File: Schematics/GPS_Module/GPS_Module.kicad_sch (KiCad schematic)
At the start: 21 parts, among them U1 STM32F103CBTx, U2 ISO1042BQDWVQ1, U3 SAM-M10Q, Y1 16MHz

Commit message: added notes
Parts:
- removed D3: STATUS_LED, LED_SMD:LED_0805_2012Metric, symbol Device:LED
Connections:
- net +3.3V: now also C1.2, C2.2, U2.1 (VCC1), U2.4 (GND1), U2.8 (VCC2); no longer U2.5 (GND2)
- net GND1: now also U2.5 (GND2); no longer U2.4 (GND1)
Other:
- note added: "Button for reset"
- note added: "I2C PULLUP RESISTERS"
- note added: "rgb"
- moved on the sheet: C1, C2, U2

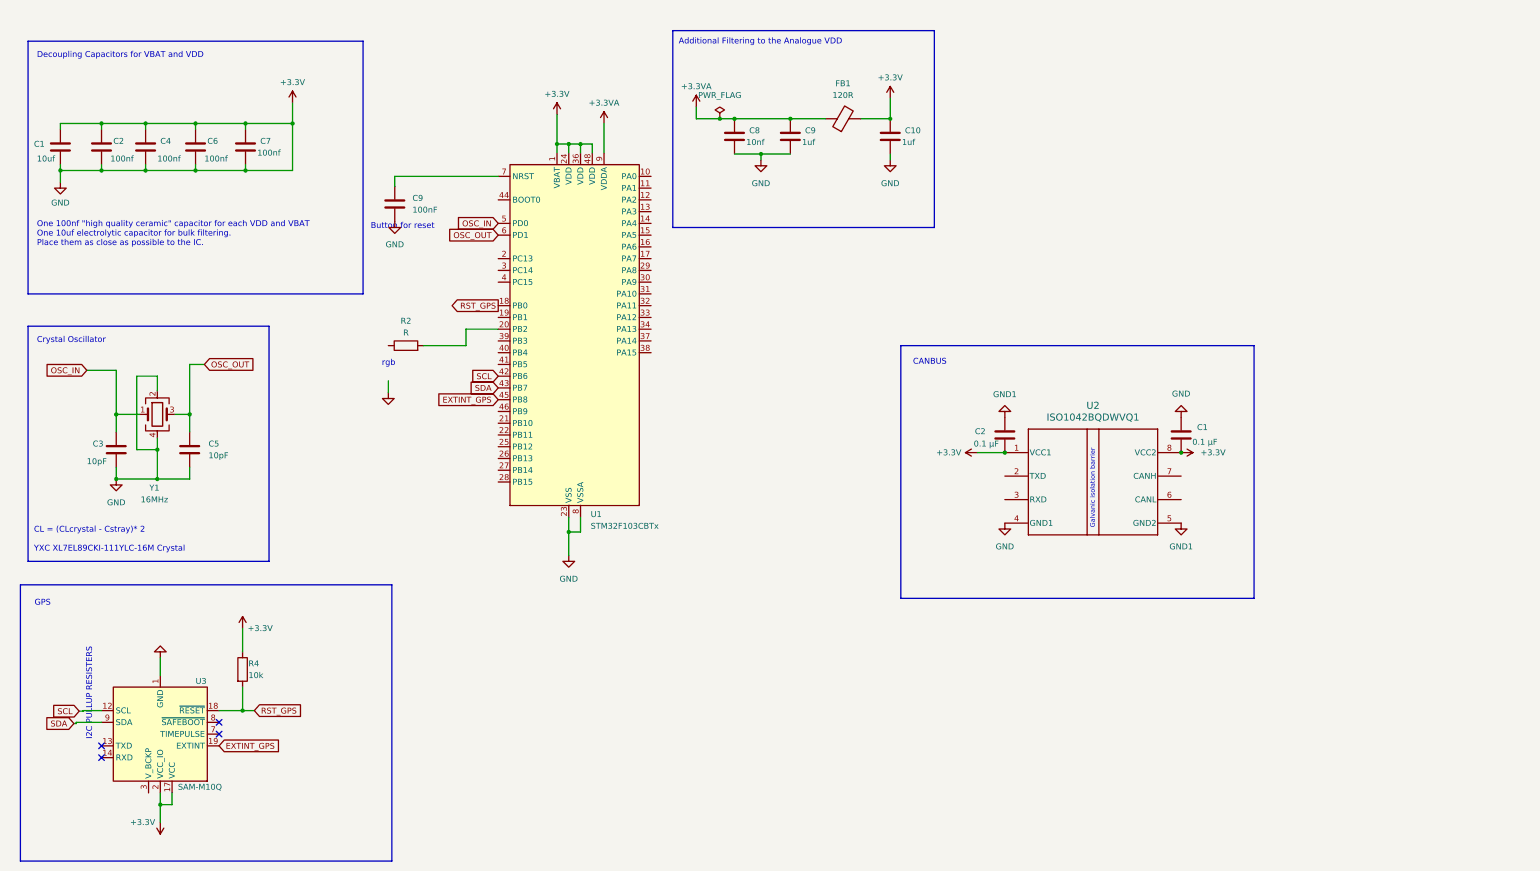
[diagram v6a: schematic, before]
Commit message: added some datasheets and schematics and updates gps module
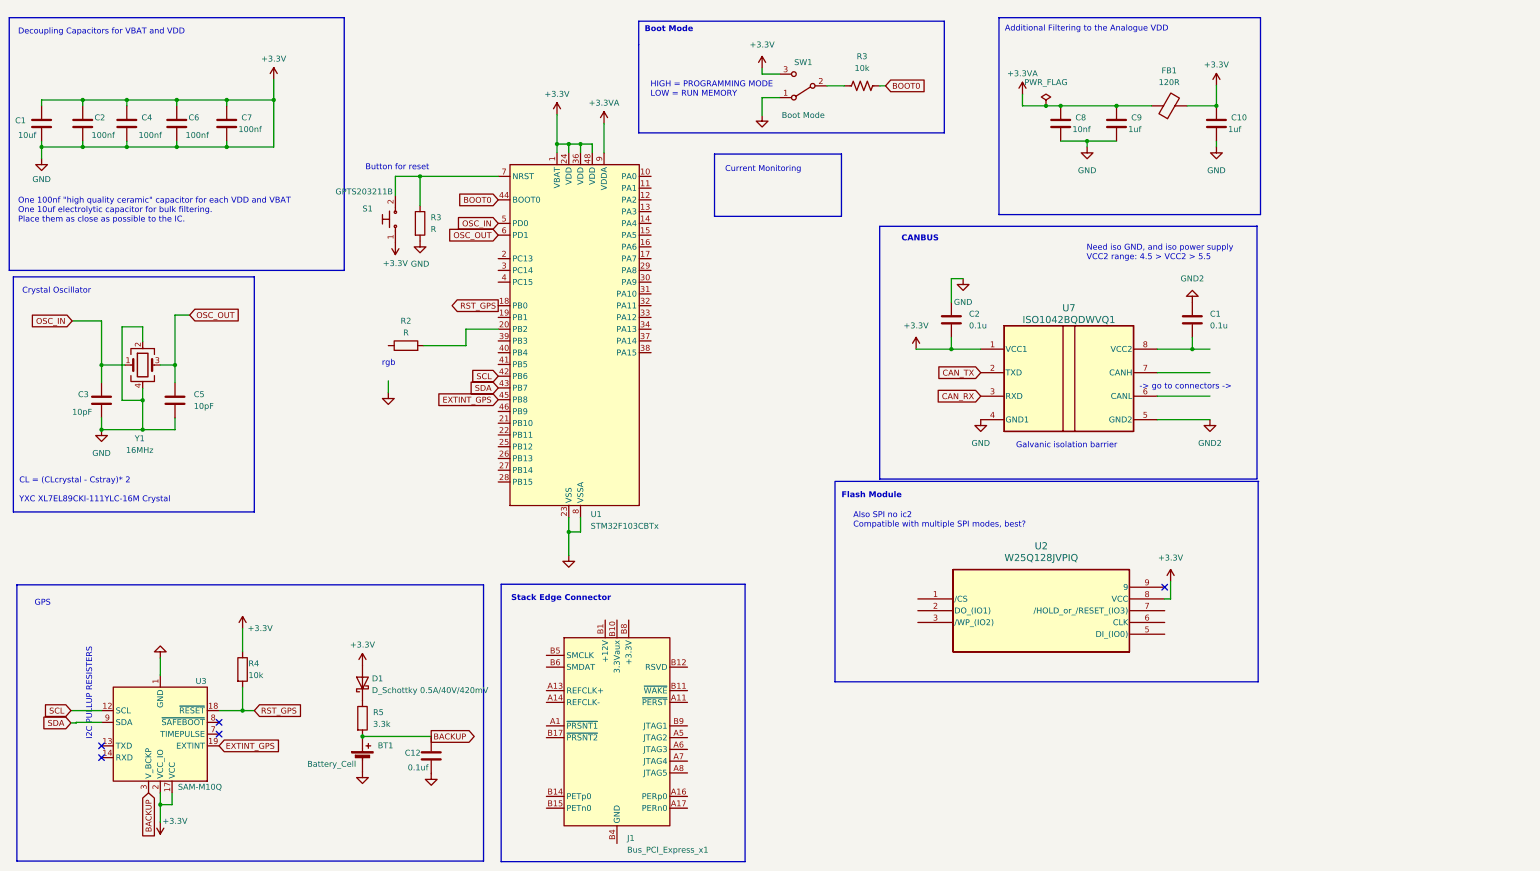
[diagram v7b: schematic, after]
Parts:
- removed C9: 100nF, Capacitor_SMD:C_0805_2012Metric, symbol Device:C
- removed U2: ISO1042BQDWVQ1, DWV0008A-IPC_A, symbol 2023-11-16_23-22-44:ISO1042BQDWVQ1
- added BT1: Battery_Cell, symbol Device:Battery_Cell
- added C12: 0.1uf, Capacitor_THT:C_Radial_D5.0mm_H11.0mm_P2.00mm, symbol Device:C
- added D1: D_Schottky 0.5A/40V/420mV, symbol Device:D_Schottky
- added J1: Bus_PCI_Express_x1, Connector_PCBEdge:BUS_PCIexpress_x1, symbol Connector:Bus_PCI_Express_x1
- added R3: R, symbol Device:R
- added R3: 10k, symbol Device:R_US
- added R5: 3.3k, symbol Device:R
- added S1: GPTS203211B, digikey-footprints:PushButton_12x12mm_THT_GPTS203211B, symbol dk_Pushbutton-Switches:GPTS203211B
- added SW1: Boot Mode, symbol Switch:SW_SPDT
- added U2: W25Q128JVPIQ, symbol QRET_Buck_PSU:W25Q128JVPIQ
- added U7: ISO1042BQDWVQ1, symbol QRET_CANBUS:ISO1042BQDWVQ1
- C1, C2: value 0.1 µF -> 0.1u
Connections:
- net GND1 is gone; now on net +3.3V: C2.1
- net +3.3V: now also BT1.2 (-), C12.2, D1.2 (A), R3.2, S1.1, SW1.1 (A), SW1.3 (C), U2.8 (VCC), U7.1 (VCC1), U7.4 (GND1); no longer C1.1, C1.2
- net at U1.7 (NRST): now also R3.1, S1.2
- net BOOT0: now reaches U1.44 (BOOT0)
- net BOOT0: now also R3.2
- net BACKUP: now reaches U3.3 (V_BCKP)
- net BACKUP: now also BT1.1 (+), C12.1, R5.2
- new net: C1.2, U7.8 (VCC2)
- new net: D1.1 (K), R5.1
- new net: R3.1, SW1.2 (B)
- new net: J1.A10 (+3.3V), J1.A9 (+3.3V), J1.B8 (+3.3V)
- new net: J1.A12 (GND), J1.A15 (GND), J1.A18 (GND), J1.A4 (GND), J1.B13 (GND), J1.B16 (GND), J1.B18 (GND), J1.B4 (GND), J1.B7 (GND)
- new net: J1.A2 (+12V), J1.A3 (+12V), J1.B1 (+12V), J1.B2 (+12V), J1.B3 (+12V)
- new net CAN_RX: U7.3 (RXD)
- new net CAN_TX: U7.2 (TXD)
- new net GND2: C1.1, U7.5 (GND2)
- no-connect marks 4 -> 5
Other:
- note added: "-> go to connectors ->"
- note added: "Also SPI no ic2 Compatible with multiple SPI modes, best?"
- note added: "Boot Mode"
- note added: "Current Monitoring"
- note added: "Flash Module"
- note added: "HIGH = PROGRAMMING MODE LOW = RUN MEMORY"
- note added: "Need iso GND, and iso power supply VCC2 range: 4.5 > VCC2 > 5.5"
- note added: "Stack Edge Connector"
- moved on the sheet: C1, C10, C2, C3, C4, C5, C6, C7, C8, C9, FB1, Y1

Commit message: updarted module and added schematic files
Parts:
- removed R3: R, symbol Device:R
- added C13: 0.1uF, Capacitor_SMD:C_0402_1005Metric, symbol Device:C
- added C15: 100nF, Capacitor_SMD:C_0603_1608Metric, symbol Device:C
- added C15: 0.1uf, Capacitor_SMD:C_0402_1005Metric, symbol Device:C
- added D2: LTST-C190KSKT, digikey-footprints:0603, symbol dk_LED-Indication-Discrete:LTST-C190KSKT
- added D4: LTST-C191KRKT, digikey-footprints:LED_0603, symbol dk_LED-Indication-Discrete:LTST-C191KRKT
- added IC1: ACS70331EOLCTR-2P5U3, SOIC127P600X175-8N, symbol ACS70331EOLCTR-2P5U3:ACS70331EOLCTR-2P5U3
- added R10, R11, R6, R7: 2.2k, symbol Device:R
- added R11, R12: 10k, Resistor_SMD:R_0603_1608Metric, symbol Device:R
- added R8, R9: 22, symbol Device:R
- added U5: LM66100DCKR, DCK6_TEX, symbol 2024-01-25_02-56-12:LM66100DCKR
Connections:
- net +3.3V: now also S1.2, C13.2, C15.1, C15.2, D2.2, D4.1, IC1.3 (IP-_1), IC1.4 (IP-_2), IC1.5 (GND), R10.1, R11.1, R11.2, R12.1, R7.2; no longer S1.1
- net SCL: now also R10.2, R8.2; no longer U3.12 (SCL)
- net SDA: now also R11.2, R9.2; no longer U3.9 (SDA)
- net at U1.7 (NRST): now also S1.1, C13.1; no longer S1.2
- net CANL: now reaches U7.6 (CANL)
- net CANH: now reaches U7.7 (CANH)
- net CS_FL: now reaches U2.1 (/CS)
- net MISO_FL: now reaches U2.2 (DO_(IO1))
- net at U2.3 (/WP_(IO2)): now also R11.1
- net MOSI_FL: now reaches U2.5 (DI_(IO0))
- net SCK_FL: now reaches U2.6 (CLK)
- net RESET_FL: now reaches U2.7 (/HOLD_or_/RESET_(IO3))
- net RESET_FL: now also R12.2
- net PPS: now reaches U3.7 (TIMEPULSE)
- net PPS: now also R6.2
- new net: IC1.1 (IP+_1), IC1.2 (IP+_2)
- new net: C15.1, IC1.8 (VCC)
- new net: D2.1, R6.1
- new net: D4.2, R7.1
- new net: R8.1, U3.12 (SCL)
- new net: R9.1, U3.9 (SDA)
- new net VDOUT: C15.2
- new net VIOUT: IC1.7 (VIOUT)
- no-connect marks 5 -> 6
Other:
- moved on the sheet: BT1, C12, D1, J1, R2, R3, R5, S1, SW1, U1, U2
